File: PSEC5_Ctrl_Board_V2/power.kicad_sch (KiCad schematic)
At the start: 36 parts

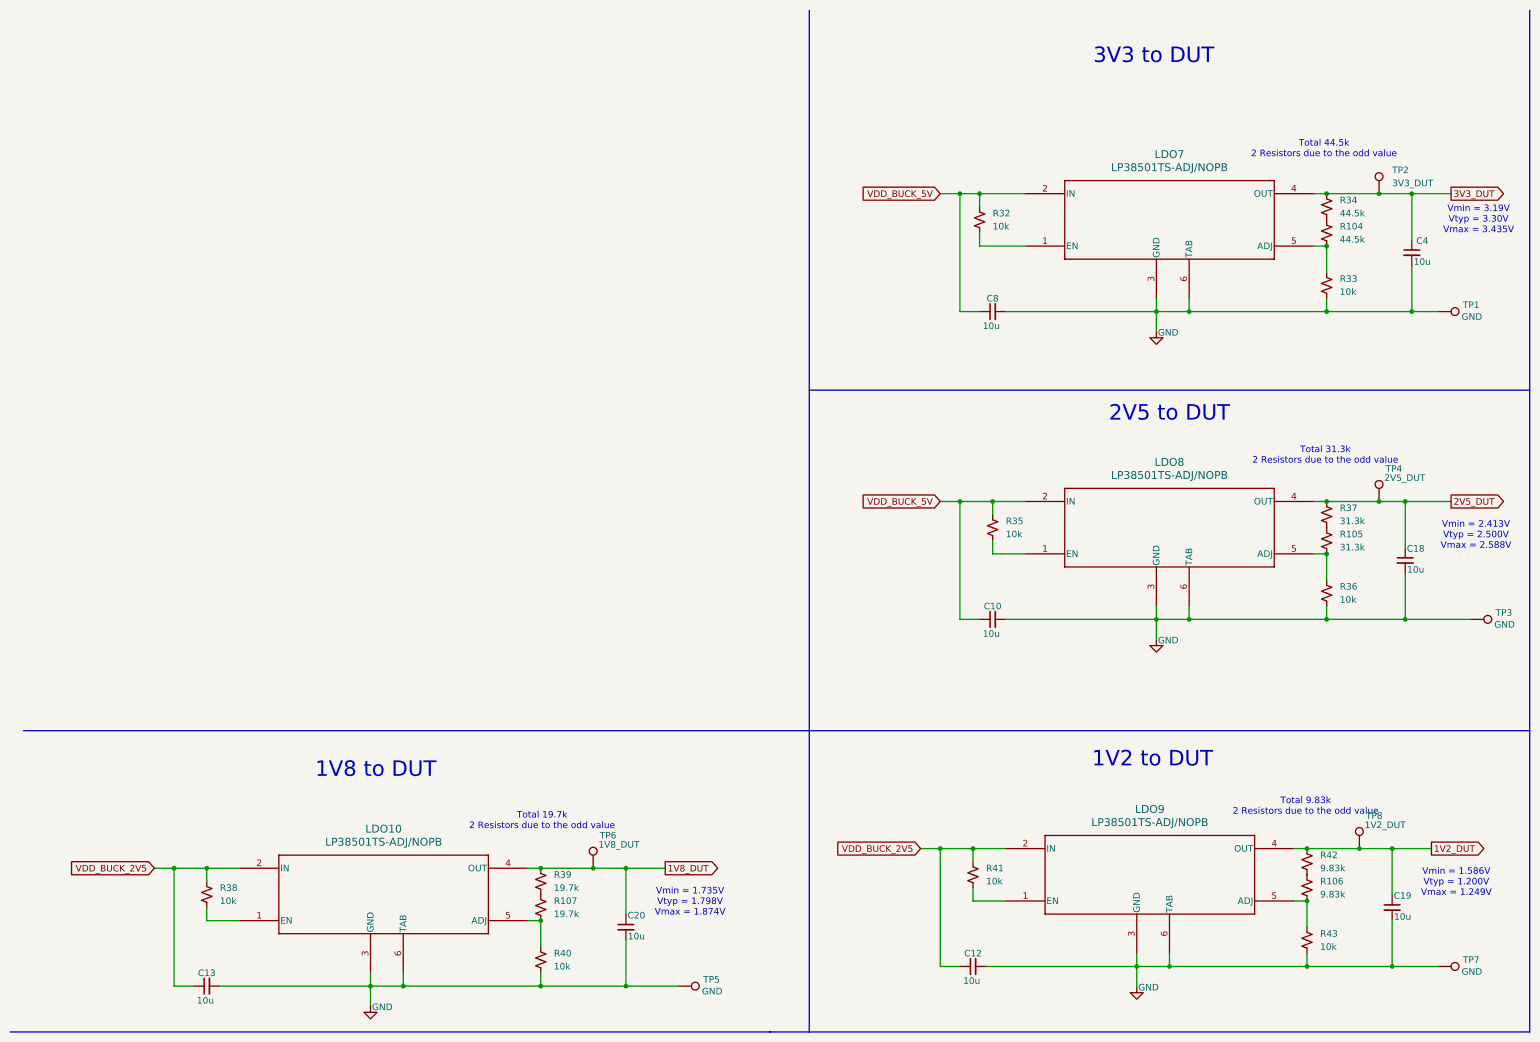
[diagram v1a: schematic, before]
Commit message: V2 Ready for Review
Everything added and new trace thickness + changes, Still need to add 5mm standoff pads, however I don't belive the measurements on the datasheet so I will review other parts first. Soldermask maybe needs some work too
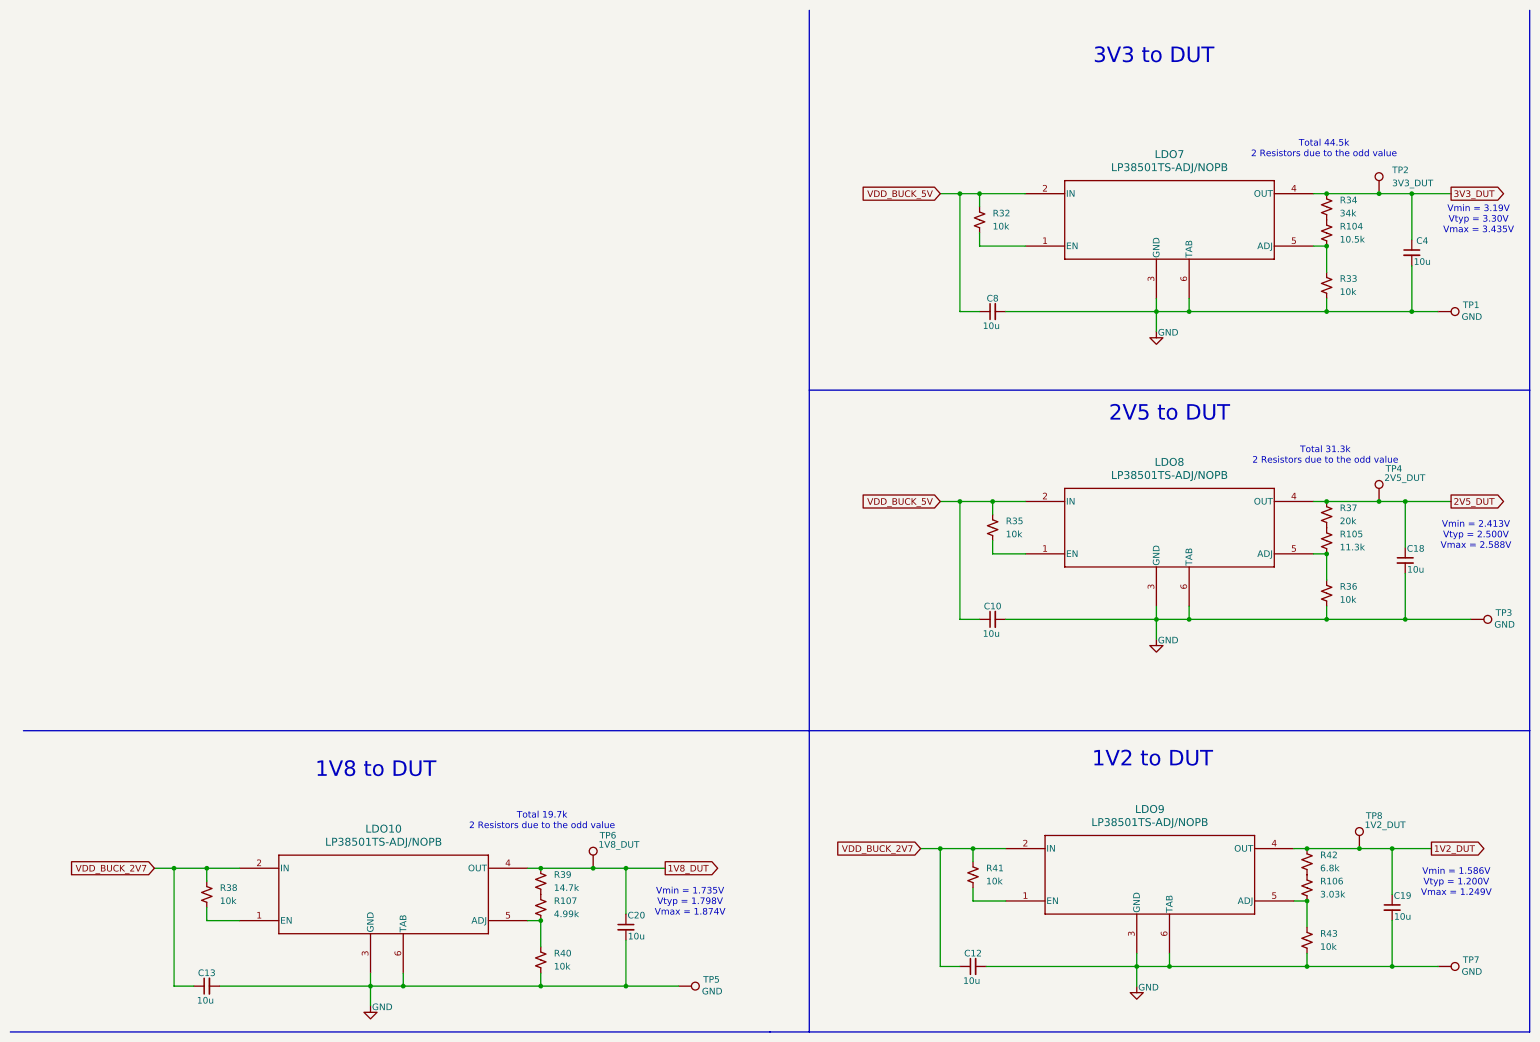
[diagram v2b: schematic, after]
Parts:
- R104: value 44.5k -> 10.5k
- R105: value 31.3k -> 11.3k
- R106: value 9.83k -> 3.03k
- R107: value 19.7k -> 4.99k
- R34: value 44.5k -> 34k
- R37: value 31.3k -> 20k
- R39: value 19.7k -> 14.7k
- R42: value 9.83k -> 6.8k
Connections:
- net VDD_BUCK_2V5 renamed VDD_BUCK_2V7
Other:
- note removed: "Total 9.83k 2 Resistors due to the odd value"
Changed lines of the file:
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@@
 		)
 	)
-	(text "Total 9.83k\n2 Resistors due to the odd value\n"
-		(exclude_from_sim no)
-		(at 261.366 167.132 0)
-		(effects
-			(font
-				(size 1.27 1.27)
-			)
-		)
-	)
 	(text "Total 31.3k\n2 Resistors due to the odd value\n"
 		(exclude_from_sim no)
@@
 		)
 	)
-	(global_label "VDD_BUCK_2V5"
+	(global_label "VDD_BUCK_2V7"
 		(shape input)
 		(at 38.1 179.07 180)
@@
 		)
 	)
-	(global_label "VDD_BUCK_2V5"
+	(global_label "VDD_BUCK_2V7"
 		(shape input)
 		(at 186.69 175.26 180)
@@
 			)
 		)
-		(property "Value" "44.5k"
+		(property "Value" "10.5k"
 			(at 267.97 57.1499 0)
 			(effects
@@
 			)
 		)
-		(property "Value" "9.83k"
+		(property "Value" "6.8k"
 			(at 264.16 179.0699 0)
 			(effects
@@
 			)
 		)
-		(property "Value" "19.7k"
+		(property "Value" "4.99k"
 			(at 115.57 187.9599 0)
 			(effects
@@
 			)
 		)
-		(property "Value" "9.83k"
+		(property "Value" "3.03k"
 			(at 264.16 184.1499 0)
 			(effects
@@
 			)
 		)
-		(property "Value" "44.5k"
+		(property "Value" "34k"
 			(at 267.97 52.0699 0)
 			(effects
@@
 			)
 		)
-		(property "Value" "19.7k"
+		(property "Value" "14.7k"
 			(at 115.57 182.8799 0)
 			(effects
@@
 			)
 		)
-		(property "Value" "31.3k"
+		(property "Value" "20k"
 			(at 267.97 111.7599 0)
 			(effects
@@
 			)
 		)
-		(property "Value" "31.3k"
+		(property "Value" "11.3k"
 			(at 267.97 116.8399 0)
 			(effects

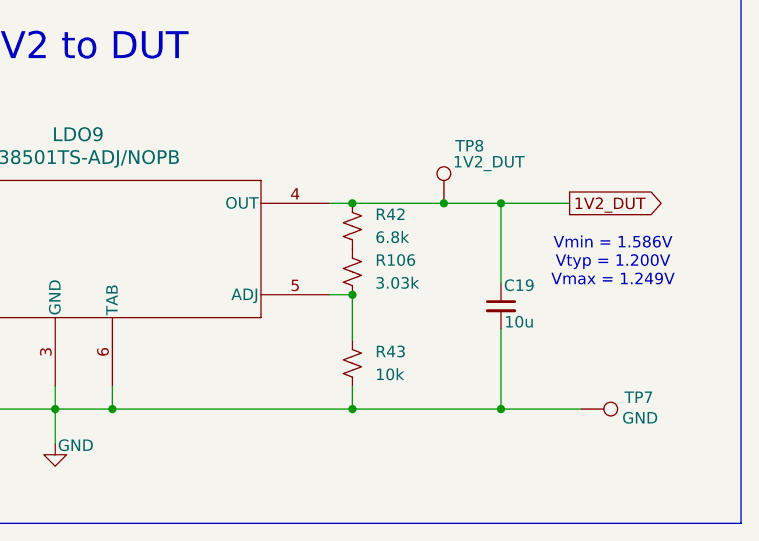
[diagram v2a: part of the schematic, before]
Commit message: Updated many values on schematic to match BOM
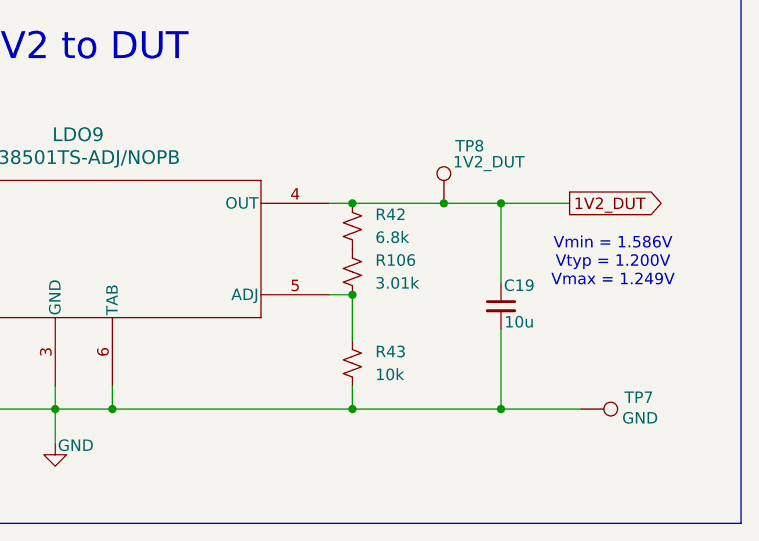
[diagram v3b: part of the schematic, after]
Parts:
- R106: value 3.03k -> 3.01k
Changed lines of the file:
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@@
 			)
 		)
-		(property "Value" "3.03k"
+		(property "Value" "3.01k"
 			(at 264.16 184.1499 0)
 			(effects
